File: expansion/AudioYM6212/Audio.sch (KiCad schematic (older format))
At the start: 4 parts

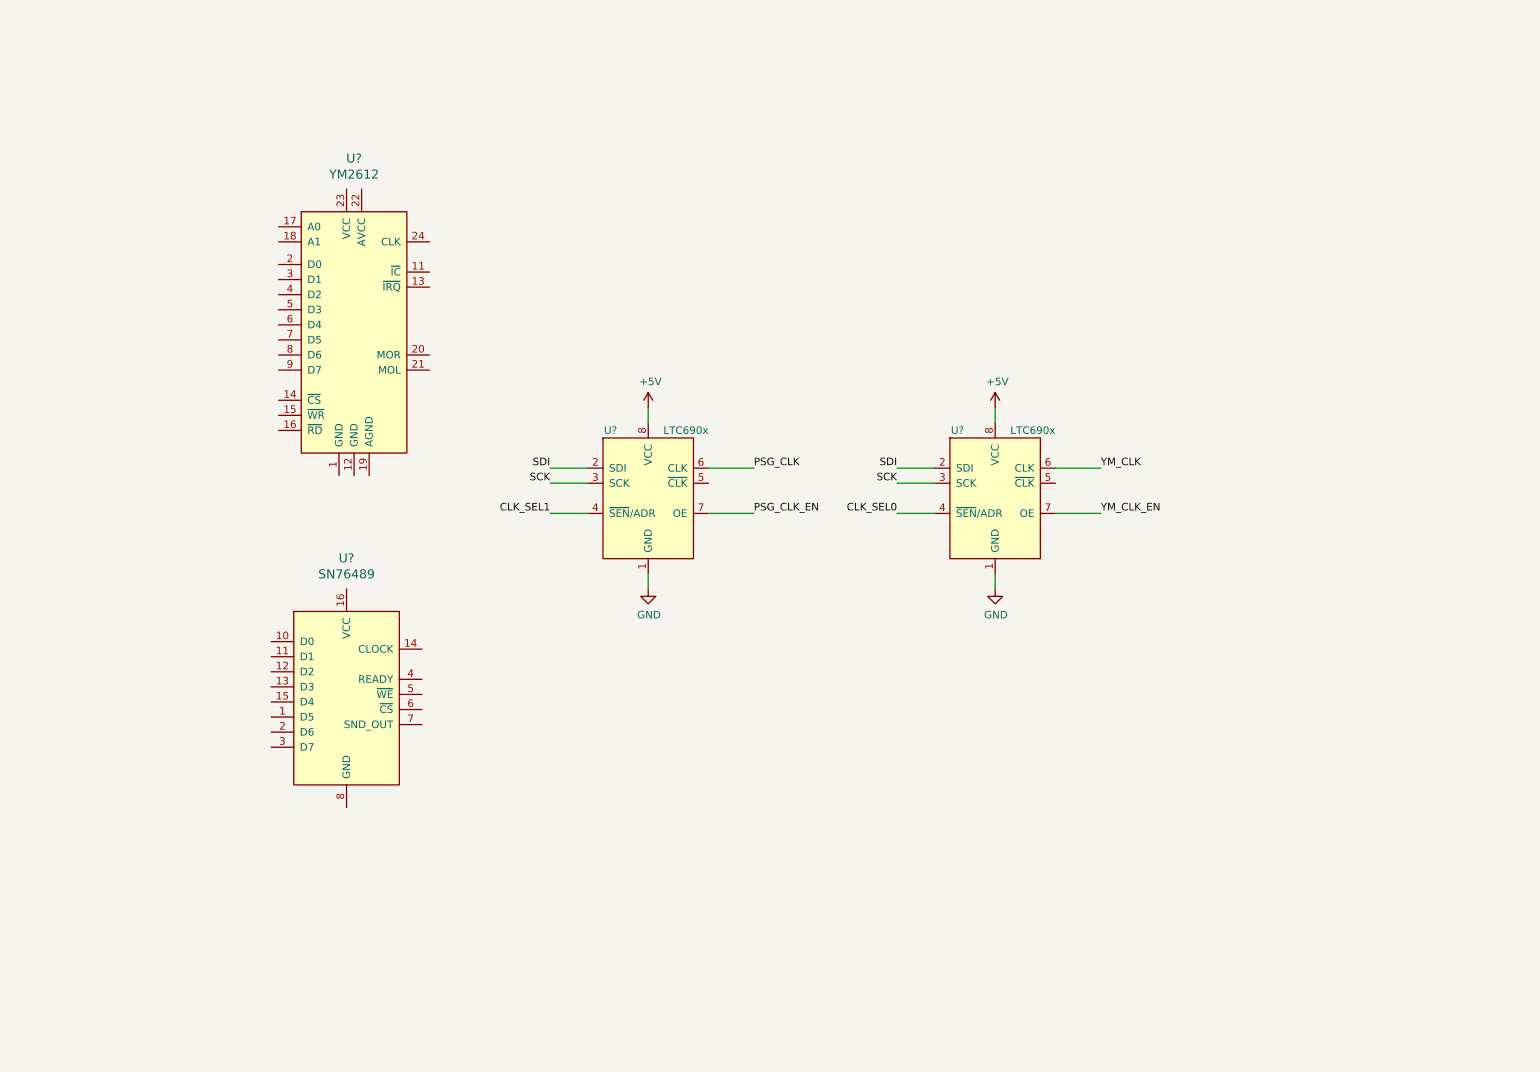
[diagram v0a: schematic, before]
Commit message: Added Eth8019 and updated page description for all projects
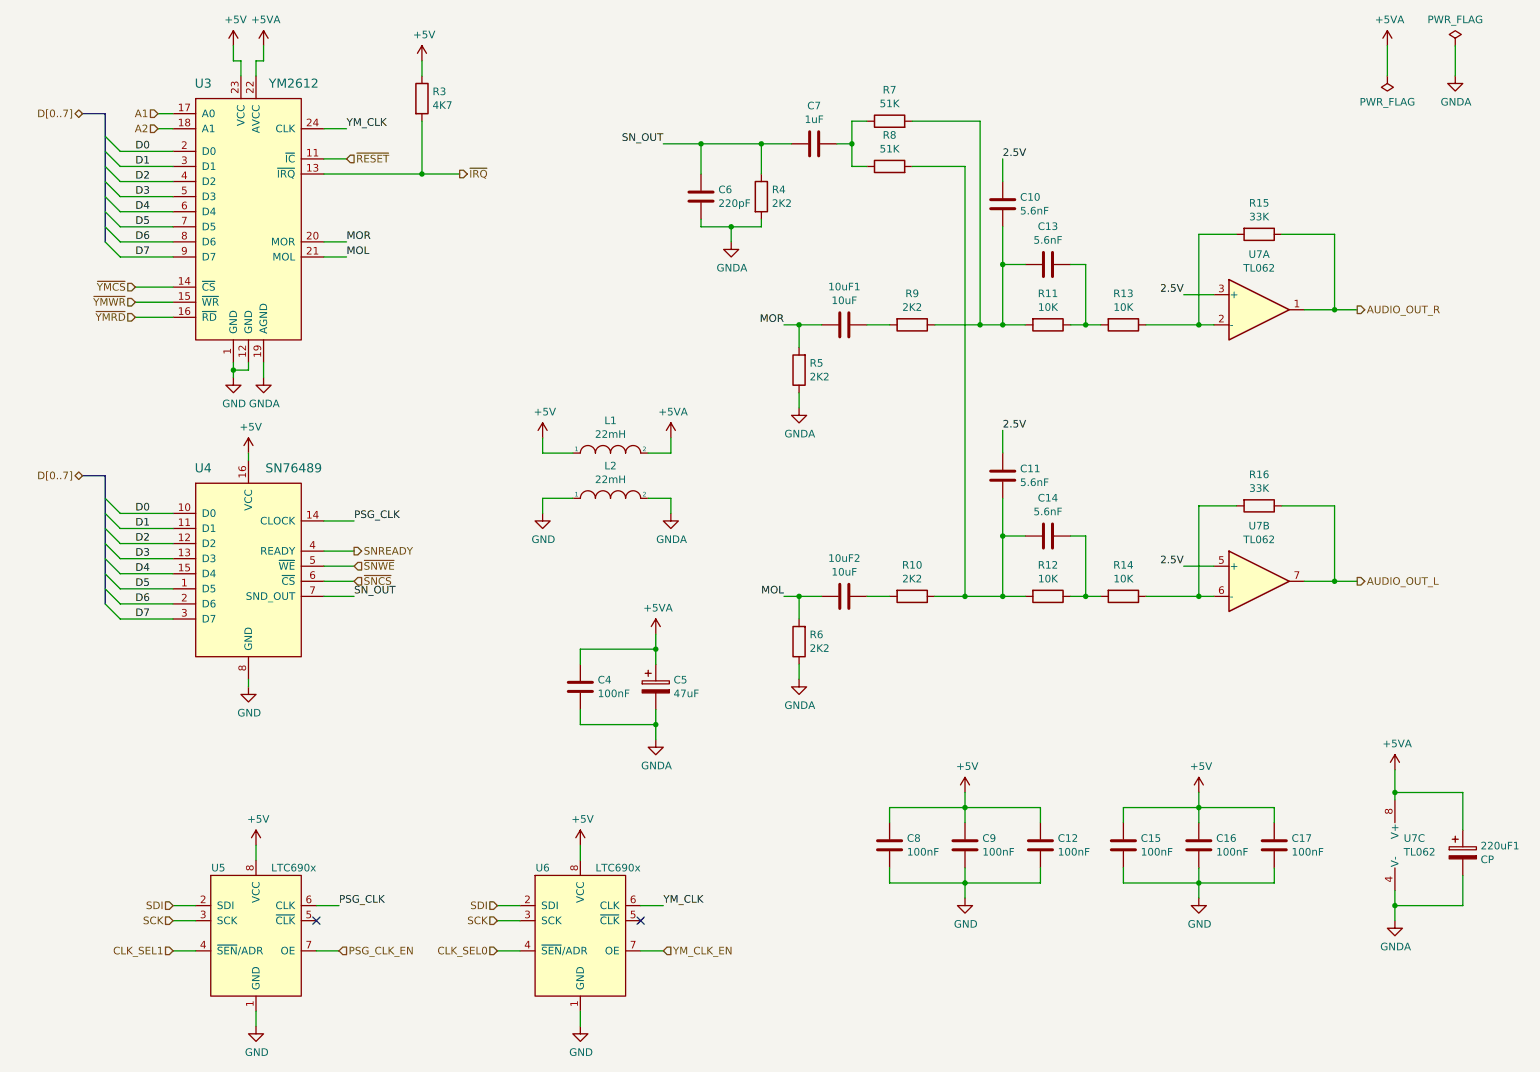
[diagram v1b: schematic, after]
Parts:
- added 10uF1, 10uF2: 10uF, symbol Device:C
- added 220uF1: CP, symbol Device:CP
- added C10, C11, C13, C14: 5.6nF, symbol Device:C
- added C12, C15, C16, C17, C4, C8, C9: 100nF, symbol Device:C
- added C5: 47uF, symbol Device:CP
- added C6: 220pF, symbol Device:C
- added C7: 1uF, symbol Device:C
- added L1, L2: 22mH, symbol pspice:INDUCTOR
- added R10, R4, R5, R6, R9: 2K2, symbol Device:R
- added R11, R12, R13, R14: 10K, symbol Device:R
- added R15, R16: 33K, symbol Device:R
- added R3: 4K7, symbol Device:R
- added R7, R8: 51K, symbol Device:R
- added U7: TL062, symbol Amplifier_Operational:TL062
- gave numbers to parts that had none: 4
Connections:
- net +5V: now also U3.23 (VCC), U4.16 (VCC), C12.1, C15.1, C16.1, C17.1, C8.1, C9.1, L1.1, R3.1
- net GND: now also U3.1 (GND), U3.12 (GND), U4.8 (GND), C12.2, C15.2, C16.2, C17.2, C8.2, C9.2, L2.1
- net PSG_CLK: now also U4.14 (CLOCK)
- net YM_CLK: now also U3.24 (CLK)
- net ~RESET: now reaches U3.11 (~IC)
- net ~IRQ: now reaches U3.13 (~IRQ)
- net ~IRQ: now also R3.2
- net ~YMCS: now reaches U3.14 (~CS)
- net ~YMWR: now reaches U3.15 (~WR)
- net ~YMRD: now reaches U3.16 (~RD)
- net A1: now reaches U3.17 (A0)
- net A2: now reaches U3.18 (A1)
- net GNDA: now reaches U3.19 (AGND)
- net GNDA: now also 220uF1.2, C4.2, C5.2, C6.2, L2.2, R4.2, R5.1, R6.1, U7.4 (V-)
- net D0: now reaches U3.2 (D0)
- net D0: now also U4.10 (D0)
- net MOR: now reaches U3.20 (MOR)
- net MOR: now also 10uF1.2, R5.2
- net MOL: now reaches U3.21 (MOL)
- net MOL: now also 10uF2.2, R6.2
- net +5VA: now reaches U3.22 (AVCC)
- net +5VA: now also 220uF1.1, C4.1, C5.1, L1.2, U7.8 (V+)
- net D1: now reaches U3.3 (D1)
- net D1: now also U4.11 (D1)
- net D2: now reaches U3.4 (D2)
- net D2: now also U4.12 (D2)
- net D3: now reaches U3.5 (D3)
- net D3: now also U4.13 (D3)
- net D4: now reaches U3.6 (D4)
- net D4: now also U4.15 (D4)
- net D5: now reaches U3.7 (D5)
- net D5: now also U4.1 (D5)
- net D6: now reaches U3.8 (D6)
- net D6: now also U4.2 (D6)
- net D7: now reaches U3.9 (D7)
- net D7: now also U4.3 (D7)
- net SNREADY: now reaches U4.4 (READY)
- net ~SNWE: now reaches U4.5 (~WE)
- net ~SNCS: now reaches U4.6 (~CS)
- net SN_OUT: now reaches U4.7 (SND_OUT)
- net SN_OUT: now also C6.1, C7.2, R4.1
- new net: R13.1, R15.2, U7.2 (-)
- new net: R14.1, R16.2, U7.6 (-)
- new net: C13.1, R11.1, R13.2
- new net: C10.2, C13.2, R11.2, R7.2, R9.1
- new net: 10uF1.1, R9.2
- new net: C14.1, R12.1, R14.2
- new net: C11.2, C14.2, R10.1, R12.2, R8.2
- new net: 10uF2.1, R10.2
- new net: C7.1, R7.1, R8.1
- new net 2.5V: C10.1, C11.1, U7.3 (+), U7.5 (+)
- new net AUDIO_OUT_L: R16.1, U7.7
- new net AUDIO_OUT_R: R15.1, U7.1
- no-connect marks 0 -> 2
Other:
- moved on the sheet: U3, U4, U5, U6

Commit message: Working on YM2612 layout
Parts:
- C10: renamed from C8; footprint (none) -> Capacitor_THT:C_Disc_D5.0mm_W2.5mm_P2.50mm
- C11: renamed from C9; footprint (none) -> Capacitor_THT:C_Disc_D5.0mm_W2.5mm_P2.50mm
- C12: renamed from C10; footprint (none) -> Capacitor_THT:C_Disc_D5.0mm_W2.5mm_P2.50mm
- C13: renamed from C11; footprint (none) -> Capacitor_THT:C_Disc_D5.0mm_W2.5mm_P2.50mm
- C14: renamed from C12; footprint (none) -> Capacitor_THT:C_Disc_D5.0mm_W2.5mm_P2.50mm
- C15: renamed from C13; footprint (none) -> Capacitor_THT:C_Disc_D5.0mm_W2.5mm_P2.50mm
- C16: renamed from C14; footprint (none) -> Capacitor_THT:C_Disc_D5.0mm_W2.5mm_P2.50mm
- C17: renamed from C15; footprint (none) -> Capacitor_THT:C_Disc_D5.0mm_W2.5mm_P2.50mm
- C18: renamed from C16; footprint (none) -> Capacitor_THT:C_Disc_D5.0mm_W2.5mm_P2.50mm
- C19: renamed from C17; footprint (none) -> Capacitor_THT:C_Disc_D5.0mm_W2.5mm_P2.50mm
- C20: renamed from 220uF1; value CP -> 220uF; footprint (none) -> Capacitor_THT:CP_Radial_D5.0mm_P2.50mm
- C4, C6, C7: footprint (none) -> Capacitor_THT:C_Disc_D5.0mm_W2.5mm_P2.50mm
- C5: footprint (none) -> Capacitor_THT:CP_Radial_D5.0mm_P2.50mm
- C8: renamed from 10uF1; footprint (none) -> Capacitor_THT:C_Disc_D5.0mm_W2.5mm_P2.50mm
- C9: renamed from 10uF2; footprint (none) -> Capacitor_THT:C_Disc_D5.0mm_W2.5mm_P2.50mm
- L1, L2: footprint (none) -> Inductor_THT:L_Radial_D8.7mm_P5.00mm_Fastron_07HCP
- R10, R11, R12, R13, R14, R15, R16, R3, R4, R5, R6, R7, R8, R9: footprint (none) -> Resistor_THT:R_Axial_DIN0207_L6.3mm_D2.5mm_P10.16mm_Horizontal
- U3: footprint (none) -> Package_DIP:DIP-24_W15.24mm_Socket
- U4: footprint (none) -> Package_DIP:DIP-16_W7.62mm_Socket
- U5, U6: footprint (none) -> Ddraig:SOP65P490X110-8N
- U7: footprint (none) -> Package_DIP:DIP-8_W7.62mm_Socket
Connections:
- net GNDA: now also C6.1; no longer C6.2
- net SN_OUT: now also C6.2, C7.1; no longer C6.1, C7.2
- net at R7.1, R8.1: now also C7.2; no longer C7.1
- net D0 renamed D8
- net D1 renamed D9
- net D2 renamed D10
- net D3 renamed D11
- net D4 renamed D12
- net D5 renamed D13
- net D6 renamed D14
- net D7 renamed D15
